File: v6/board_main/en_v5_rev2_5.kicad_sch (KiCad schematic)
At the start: 8 parts, among them U8 SPARTAN7-LX15

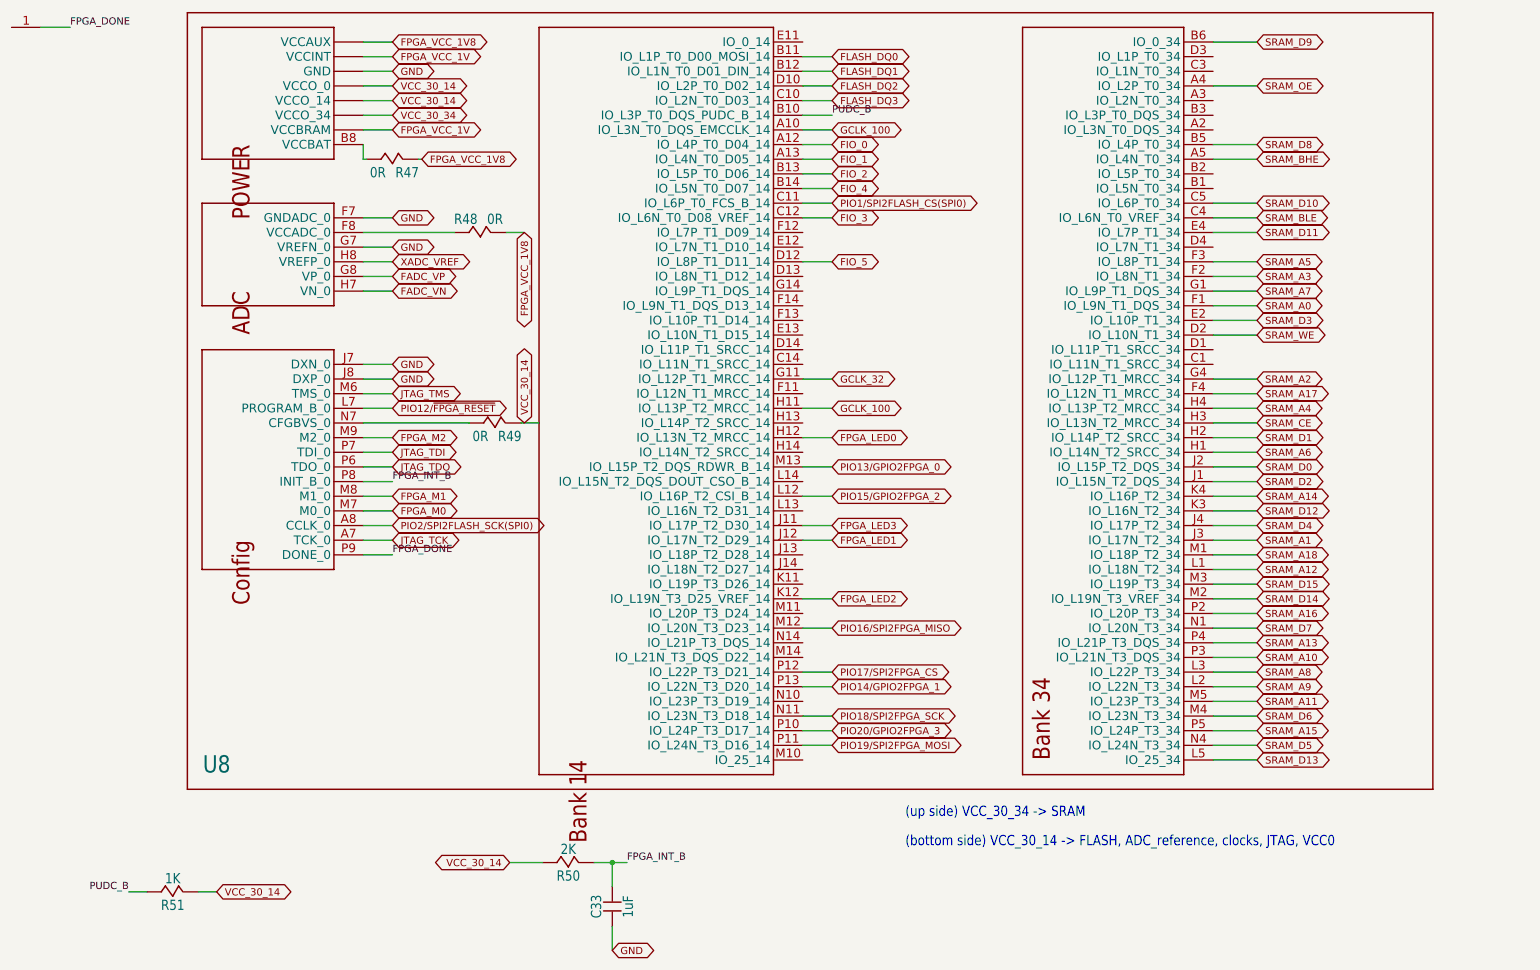
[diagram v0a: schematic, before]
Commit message: Rephrasing ENV5 design
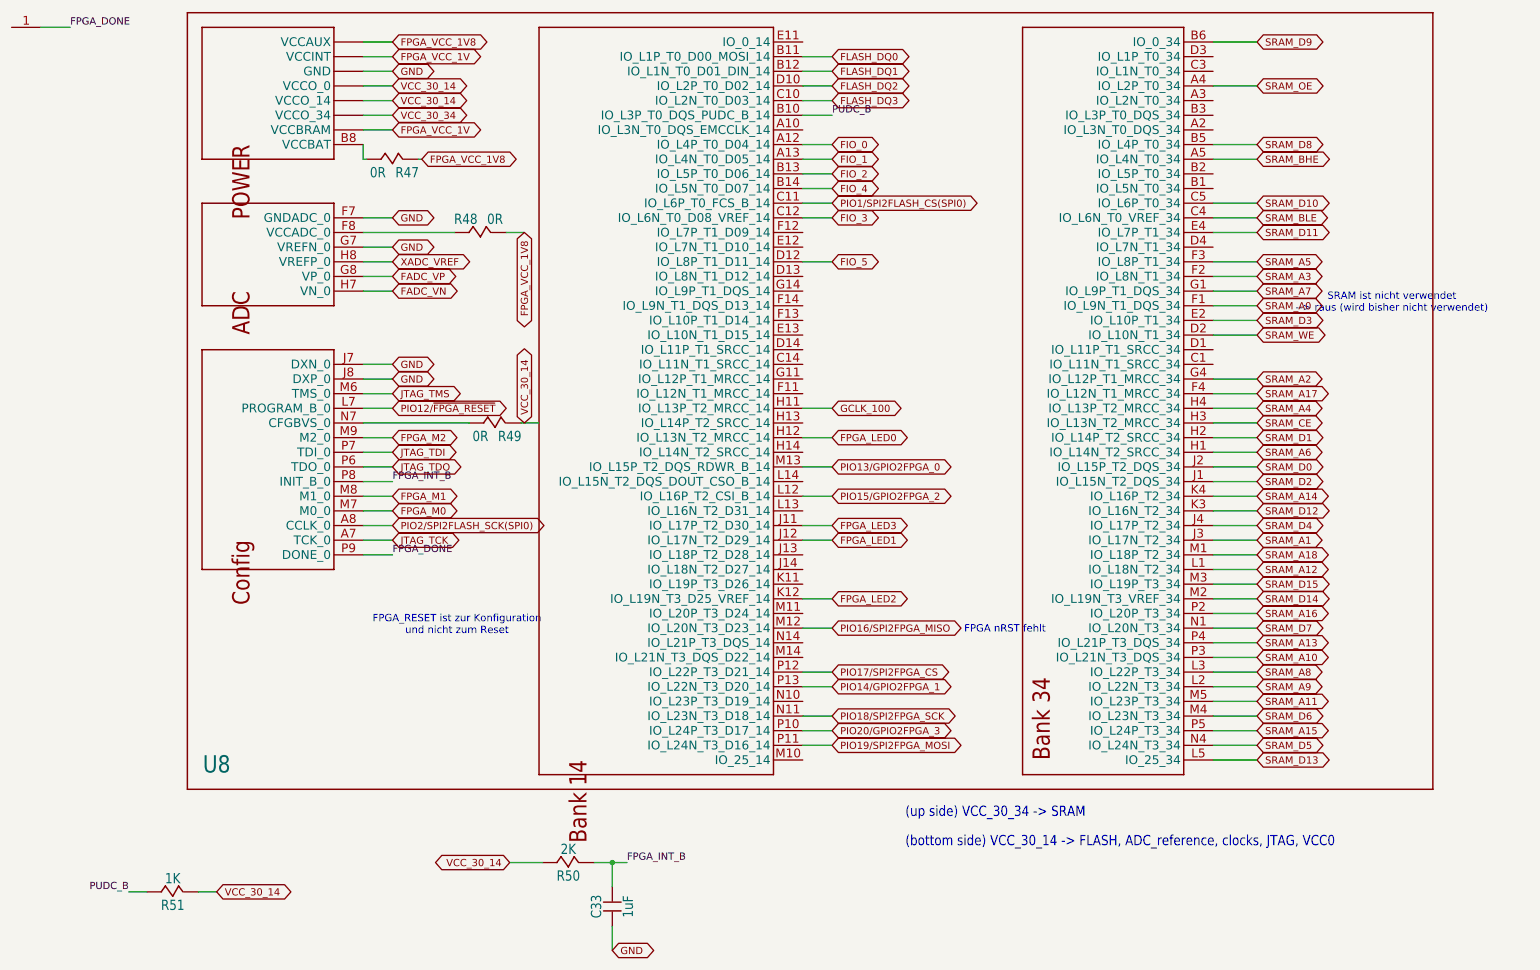
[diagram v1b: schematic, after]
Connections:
- net GCLK_100: no longer U8.A10 (IO_L3N_T0_DQS_EMCCLK_14)
- net GCLK_32: no longer names the net of U8.G11 (IO_L12P_T1_MRCC_14)
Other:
- note added: "FPGA nRST fehlt"
- note added: "FPGA_RESET ist zur Konfiguration und nicht zum Reset"
- note added: "SRAM ist nicht verwendet --> raus (wird bisher nicht verwendet)"
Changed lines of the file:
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@@
 	(generator_version "9.0")
 	(paper "User" 298.45 217.322)
+	(text "FPGA_RESET ist zur Konfiguration\nund nicht zum Reset"
+		(exclude_from_sim no)
+		(at 102.616 131.572 0)
+		(effects
+			(font
+				(size 1.27 1.27)
+			)
+		)
+	)
+	(text "SRAM ist nicht verwendet\n--> raus (wird bisher nicht verwendet)"
+		(exclude_from_sim no)
+		(at 264.668 75.692 0)
+		(effects
+			(font
+				(size 1.27 1.27)
+			)
+		)
+	)
+	(text "FPGA nRST fehlt"
+		(exclude_from_sim no)
+		(at 197.612 132.334 0)
+		(effects
+			(font
+				(size 1.27 1.27)
+			)
+		)
+	)
 	(text "(up side) VCC_30_34 -> SRAM"
 		(exclude_from_sim no)
@@
 	(wire
 		(pts
-			(xy 162.56 88.9) (xy 167.64 88.9)
-		)
-		(stroke
-			(width 0.1524)
-			(type solid)
-		)
-	)
-	(wire
-		(pts
 			(xy 233.68 114.3) (xy 241.3 114.3)
 		)
@@
 		(pts
 			(xy 86.36 86.36) (xy 91.44 86.36)
-		)
-		(stroke
-			(width 0.1524)
-			(type solid)
-		)
-	)
-	(wire
-		(pts
-			(xy 167.64 45.72) (xy 162.56 45.72)
 		)
 		(stroke
@@
 		)
 	)
-	(global_label "GCLK_100"
-		(shape bidirectional)
-		(at 167.64 45.72 0)
-		(fields_autoplaced yes)
-		(effects
-			(font
-				(size 1.2446 1.2446)
-			)
-			(justify left)
-		)
-		(property "Intersheetrefs" "${INTERSHEET_REFS}"
-			(at 180.8997 45.72 0)
-			(effects
-				(font
-					(size 1.27 1.27)
-				)
-				(justify left)
-				(hide yes)
-			)
-		)
-	)
 	(global_label "PIO20/GPIO2FPGA_3"
 		(shape bidirectional)
@@
 			(effects
 				(font
-					(size 1.27 1.27)
-				)
-				(justify left)
-				(hide yes)
-			)
-		)
-	)
-	(global_label "GCLK_32"
-		(shape bidirectional)
-		(at 167.64 88.9 0)
-		(fields_autoplaced yes)
-		(effects
-			(font
-				(size 1.2446 1.2446)
-			)
-			(justify left)
-		)
-		(property "Intersheetrefs" "${INTERSHEET_REFS}"
-			(at 179.7144 88.9 0)
-			(effects
-				(font
